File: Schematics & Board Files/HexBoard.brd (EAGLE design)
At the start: 40.4 x 35.6 mm, 26 parts

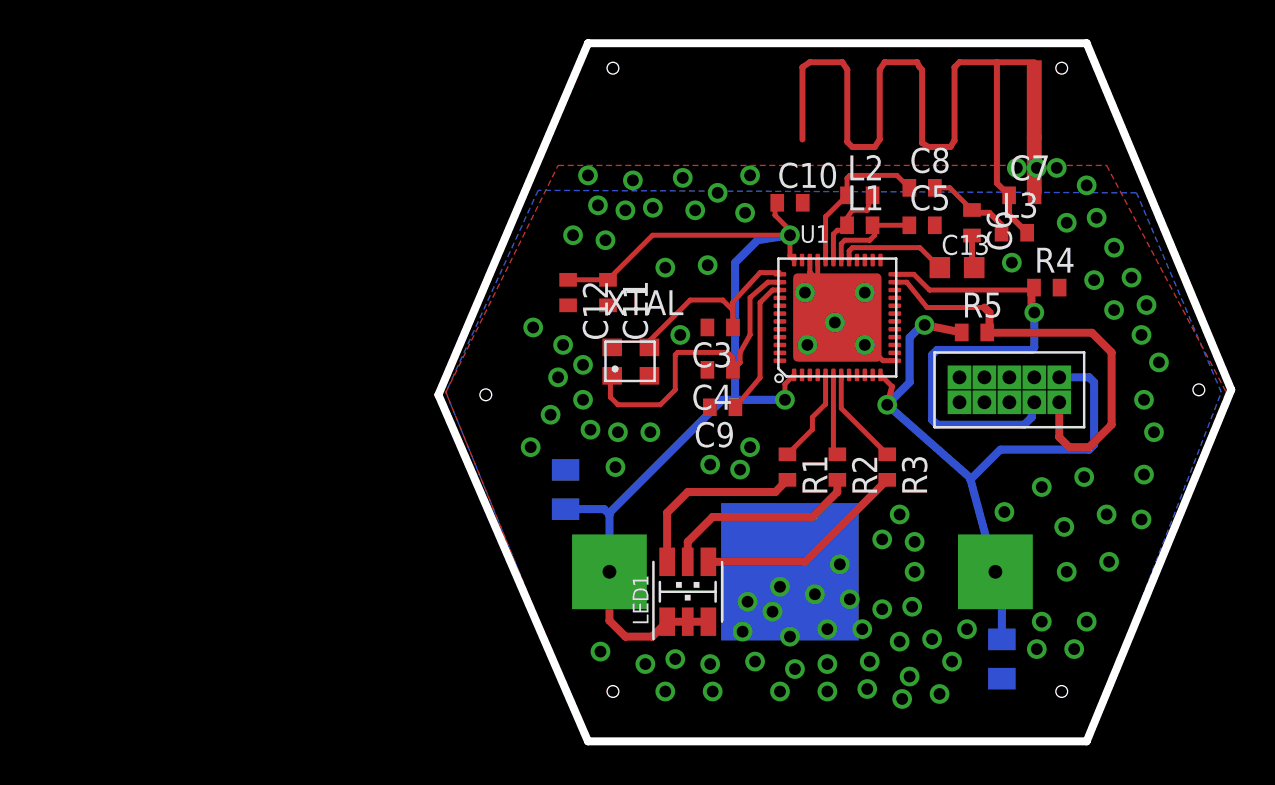
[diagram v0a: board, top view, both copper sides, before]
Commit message: Board and schematic cleanup; see email to Kris today for notes.
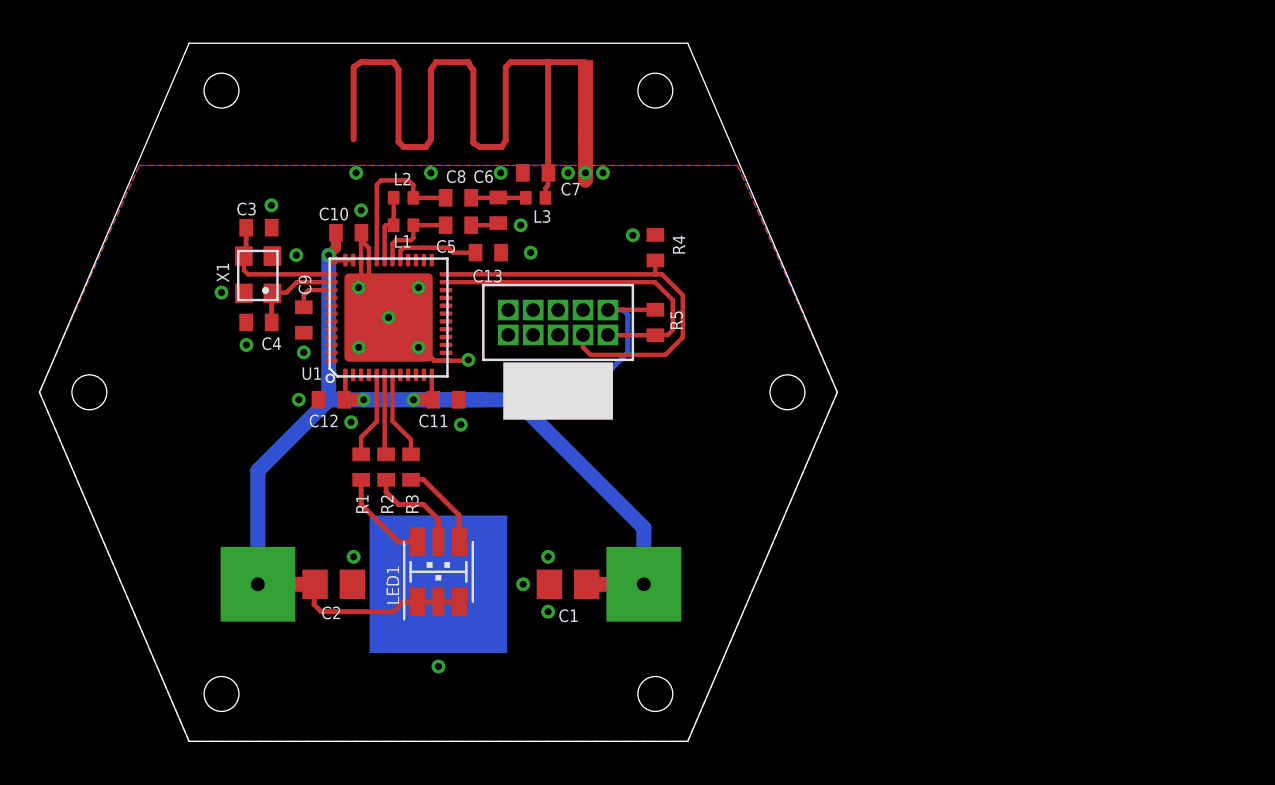
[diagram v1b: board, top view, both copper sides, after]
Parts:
- removed XTAL: TXC-CRYSTAL, TXC:TXC_CRYSTAL
- added X1: TXC-CRYSTAL, TXC:TXC_CRYSTAL
- C1, C2: device adafruit:C0805K -> rcl:C0805
- C10, C11, C12, C3, C4, C5, C6, C7, C8, C9: device adafruit:C0402 -> rcl:C0402
- C13: device adafruit:C0603K -> rcl:C0402
- L1, L2, L3: device CHIP_INDUCTOR:CHIP_INDUCTOR -> rcl_custom:.0402-B-NOSILK
- moved C7 24.8 mm to (25.3, 29.0), turned to 180 degrees
- moved R3 24.3 mm to (18.9, 14.0)
- moved C6 24.1 mm to (23.4, 27.1)
- moved C3 24.0 mm to (11.2, 26.2), turned to 0 degrees
- moved C13 23.9 mm to (22.9, 24.9)
- moved C8 23.6 mm to (21.3, 27.7)
- moved C5 23.6 mm to (21.3, 26.3)
- moved C4 23.6 mm to (11.2, 21.3)
- moved L3 23.5 mm to (25.3, 27.7)
- moved U$1 23.2 mm to (27.7, 22.0)
- moved R2 23.0 mm to (17.7, 14.0)
- moved U1 22.9 mm to (17.8, 21.6)
- moved C10 22.5 mm to (15.7, 25.9)
- moved C1 22.4 mm to (26.9, 8.00), flipped to the top, turned to 180 degrees
- moved L1 22.1 mm to (18.5, 26.3), turned to 180 degrees
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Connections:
- net N$10 renamed !RESET
- net N$7 renamed SWD
- net GND: now also X1.2, X1.4; no longer XTAL.2, XTAL.4
- net N$11: now also L1.2, L2.1; no longer L1.1, L2.2
- net N$15: now also L2.2; no longer L2.1
- net N$17: now also L1.1; no longer L1.2
- net N$8: now also X1.3; no longer XTAL.3
- net N$9: now also X1.1; no longer XTAL.1
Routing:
- net N$9: track 16.2 -> 5.39 mm
- net VDD: track 87.0 -> 78.3 mm, vias 4 -> 3
- net N$3: track 10.8 -> 4.57 mm
- net GND: track 13.0 -> 18.5 mm, vias 99 -> 29
- net !RESET: track 22.3 -> 16.9 mm
- net N$2: track 10.3 -> 5.01 mm
- net N$12: track 7.06 -> 2.12 mm
- net N$1: track 9.33 -> 4.93 mm
- net SWD: track 25.3 -> 21.6 mm, vias 1 -> 0
- net N$8: track 10.1 -> 6.89 mm
- net ANTENNA: track 40.9 -> 38.5 mm
- net N$13: track 4.58 -> 2.79 mm
- net N$18: track 5.58 -> 4.47 mm
- net N$11: track 4.62 -> 3.59 mm
- net N$17: track 5.15 -> 4.54 mm
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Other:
- board size 40.4 x 35.6 mm -> 40.6 x 35.6 mm

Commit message: Latest code latest board and schematic updated maker guide
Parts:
- removed X1: TXC-CRYSTAL, TXC:TXC_CRYSTAL
- added U$2: TXC-CRYSTAL, TXC:TXC_CRYSTAL
- moved LED1 11.4 mm to (10.0, 13.5), turned to 0 degrees
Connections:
- net GND: now also U$2.2, U$2.4; no longer X1.2, X1.4
- net N$8: now also U$2.1; no longer X1.3
- net N$9: now also U$2.3; no longer X1.1
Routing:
- net N$3: track 4.57 -> 11.1 mm
- net VDD: track 78.3 -> 83.7 mm
- net N$2: track 5.01 -> 9.80 mm
- net N$1: track 4.93 -> 8.65 mm
- net N$8: track 6.89 -> 7.42 mm
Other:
- board size 40.6 x 35.6 mm -> 40.5 x 35.6 mm
- board text added: "MIngle Disco Kris Gibbs Brandon Towell 2015"

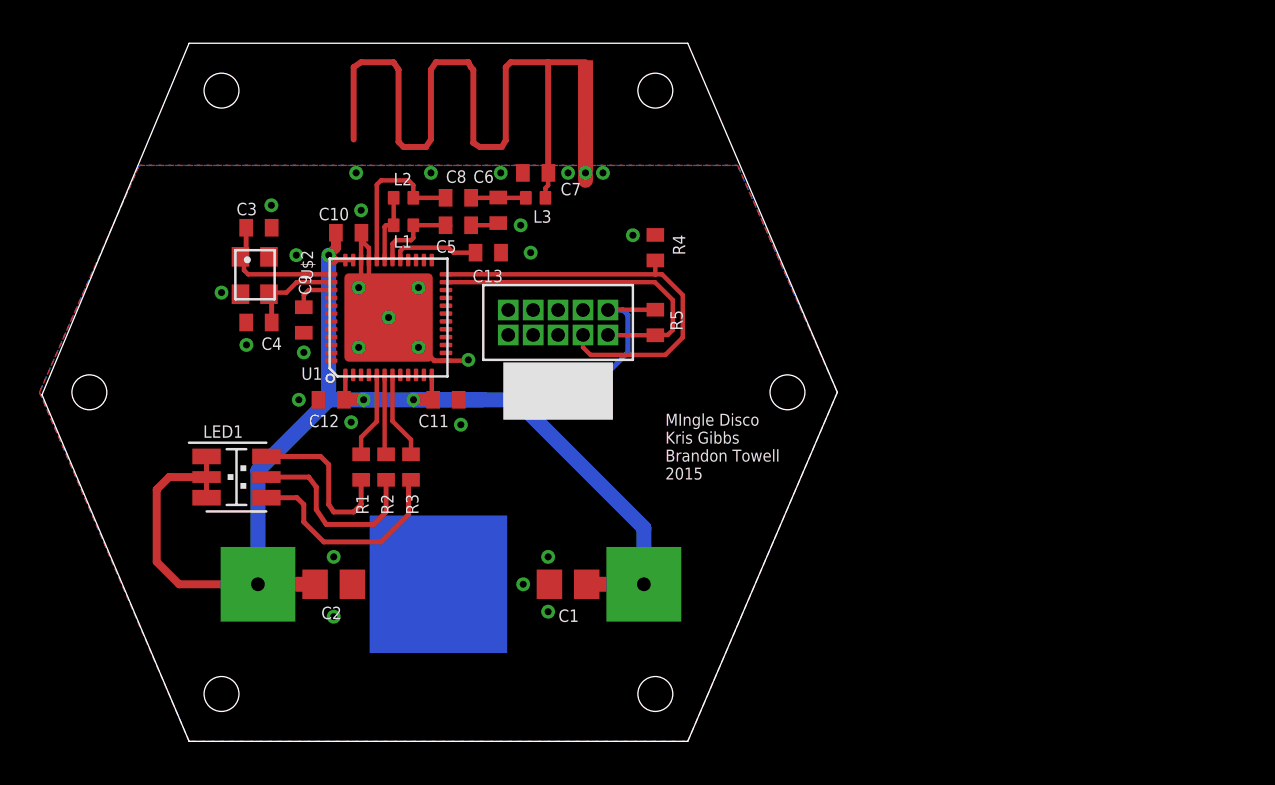
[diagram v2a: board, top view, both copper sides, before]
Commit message: OCD cleaned up of schematic -- nothing different, just prettyness. Cleaned up TNAMES layer a bit on board, checked DRC, moved a few vias... it's good to go. Sending off to OSH Parkgit add HexBoard.brd HexBoard.sch11!
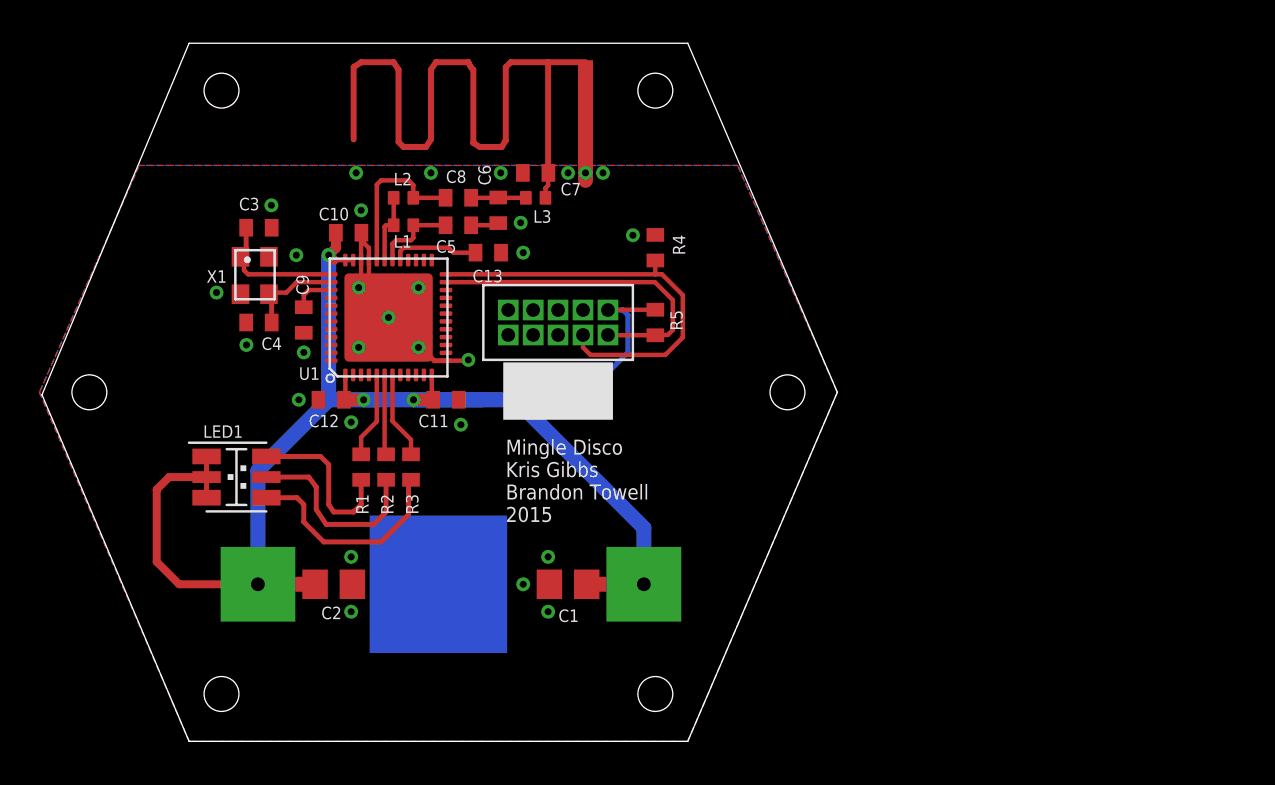
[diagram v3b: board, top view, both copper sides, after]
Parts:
- LED1: value (none) -> SMLV56RGB1W1
- U1: value (none) -> NRF51822-QFAC-R7
- X1: value TXC-CRYSTAL -> 16 MHz
- renumbered U$2 to X1
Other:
- board text added: "Mingle Disco Kris Gibbs Brandon Towell 2015"
- board text removed: "MIngle Disco Kris Gibbs Brandon Towell 2015"
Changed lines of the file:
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@@
 <?xml version="1.0" encoding="utf-8"?>
 <!DOCTYPE eagle SYSTEM "eagle.dtd">
-<eagle version="7.1.0">
+<eagle version="7.3.0">
 <drawing>
 <settings>
@@
 <layer number="14" name="Route14" color="1" fill="6" visible="no" active="yes"/>
 <layer number="15" name="Route15" color="4" fill="6" visible="no" active="yes"/>
-<layer number="16" name="Bottom" color="1" fill="1" visible="yes" active="yes"/>
+<layer number="16" name="Bottom" color="1" fill="1" visible="no" active="yes"/>
 <layer number="17" name="Pads" color="2" fill="1" visible="yes" active="yes"/>
 <layer number="18" name="Vias" color="2" fill="1" visible="yes" active="yes"/>
@@
 <layer number="20" name="Dimension" color="15" fill="1" visible="yes" active="yes"/>
 <layer number="21" name="tPlace" color="7" fill="1" visible="yes" active="yes"/>
-<layer number="22" name="bPlace" color="7" fill="1" visible="yes" active="yes"/>
+<layer number="22" name="bPlace" color="7" fill="1" visible="no" active="yes"/>
 <layer number="23" name="tOrigins" color="15" fill="1" visible="yes" active="yes"/>
 <layer number="24" name="bOrigins" color="15" fill="1" visible="no" active="yes"/>
@@
 <layer number="27" name="tValues" color="7" fill="1" visible="no" active="yes"/>
 <layer number="28" name="bValues" color="7" fill="1" visible="no" active="yes"/>
-<layer number="29" name="tStop" color="7" fill="3" visible="no" active="yes"/>
+<layer number="29" name="tStop" color="7" fill="3" visible="yes" active="yes"/>
 <layer number="30" name="bStop" color="7" fill="6" visible="no" active="yes"/>
 <layer number="31" name="tCream" color="7" fill="4" visible="no" active="yes"/>
@@
 <layer number="44" name="Drills" color="7" fill="1" visible="no" active="yes"/>
 <layer number="45" name="Holes" color="7" fill="1" visible="no" active="yes"/>
-<layer number="46" name="Milling" color="3" fill="1" visible="no" active="yes"/>
+<layer number="46" name="Milling" color="3" fill="1" visible="yes" active="yes"/>
 <layer number="47" name="Measures" color="7" fill="1" visible="no" active="yes"/>
-<layer number="48" name="Document" color="7" fill="1" visible="no" active="yes"/>
+<layer number="48" name="Document" color="7" fill="1" visible="yes" active="yes"/>
 <layer number="49" name="Reference" color="7" fill="1" visible="no" active="yes"/>
 <layer number="50" name="dxf" color="7" fill="1" visible="no" active="no"/>
-<layer number="51" name="tDocu" color="7" fill="1" visible="no" active="yes"/>
+<layer number="51" name="tDocu" color="7" fill="1" visible="yes" active="yes"/>
 <layer number="52" name="bDocu" color="7" fill="1" visible="no" active="yes"/>
 <layer number="53" name="tGND_GNDA" color="7" fill="1" visible="no" active="no"/>
@@
 <wire x1="18.034" y1="19.177" x2="17.526" y2="19.177" width="0" layer="41"/>
 <wire x1="15.367" y1="21.844" x2="15.367" y2="21.336" width="0" layer="41"/>
-<text x="31.877" y="13.335" size="0.6096" layer="25" ratio="20">MIngle Disco
+<text x="23.749" y="11.176" size="0.762" layer="25" ratio="20">Mingle Disco
 Kris Gibbs
 Brandon Towell
@@
 </autorouter>
 <elements>
-<element name="U1" library="nrf51822" package="QFN48-6X6MM" value="" x="17.78" y="21.59" smashed="yes">
-<attribute name="NAME" x="13.335" y="18.415" size="0.635" layer="25" font="vector" ratio="20"/>
+<element name="U1" library="nrf51822" package="QFN48-6X6MM" value="NRF51822-QFAC-R7" x="17.78" y="21.59" smashed="yes">
+<attribute name="NAME" x="13.208" y="18.415" size="0.635" layer="25" font="vector" ratio="20"/>
 <attribute name="VALUE" x="15.911" y="21.598" size="0.635" layer="27" ratio="10"/>
 </element>
-<element name="LED1" library="rgb-led-separate" package="LED-3528" value="" x="10.033" y="13.462" smashed="yes">
+<element name="LED1" library="rgb-led-separate" package="LED-3528" value="SMLV56RGB1W1" x="10.033" y="13.462" smashed="yes">
 <attribute name="NAME" x="8.333" y="15.462" size="0.635" layer="25" font="vector" ratio="20"/>
 <attribute name="VALUE" x="8.333" y="10.662" size="0.8" layer="27" font="vector" ratio="15"/>
@@
 </element>
 <element name="C3" library="rcl" package="C0402" value="12p" x="11.176" y="26.162" smashed="yes">
-<attribute name="NAME" x="10.033" y="26.797" size="0.635" layer="25" font="vector" ratio="20"/>
+<attribute name="NAME" x="10.16" y="27.051" size="0.635" layer="25" font="vector" ratio="20"/>
 <attribute name="VALUE" x="10.541" y="24.257" size="1.27" layer="27"/>
 </element>
@@
 </element>
 <element name="C6" library="rcl" package="C0402" value="1p" x="23.368" y="27.051" smashed="yes" rot="R270">
-<attribute name="NAME" x="22.098" y="28.448" size="0.635" layer="25" font="vector" ratio="20"/>
+<attribute name="NAME" x="22.987" y="28.321" size="0.635" layer="25" font="vector" ratio="20" rot="R90"/>
 <attribute name="VALUE" x="21.463" y="27.686" size="1.27" layer="27" rot="R270"/>
 </element>
@@
 </element>
 <element name="C9" library="rcl" package="C0402" value="100n" x="13.462" y="21.463" smashed="yes" rot="R270">
-<attribute name="NAME" x="13.843" y="22.733" size="0.635" layer="25" font="vector" ratio="20" rot="R90"/>
+<attribute name="NAME" x="13.716" y="22.733" size="0.635" layer="25" font="vector" ratio="20" rot="R90"/>
 <attribute name="VALUE" x="11.557" y="22.098" size="1.27" layer="27" rot="R270"/>
 </element>
@@
 <attribute name="NAME" x="25.273" y="27.686" size="0.2" layer="33" ratio="15" align="center"/>
 </element>
-<element name="U$2" library="TXC" package="TXC_CRYSTAL" value="TXC-CRYSTAL" x="10.795" y="23.749" rot="R270"/>
+<element name="X1" library="TXC" package="TXC_CRYSTAL" value="16 MHz" x="10.795" y="23.749" smashed="yes" rot="R270">
+<attribute name="NAME" x="8.509" y="23.36" size="0.635" layer="25" ratio="20"/>
+<attribute name="VALUE" x="8.747" y="25.019" size="0.6096" layer="27" rot="R270"/>
+</element>
 </elements>
 <signals>
@@
 <wire x1="27.813" y1="31.115" x2="27.813" y2="28.575" width="0.762" layer="1"/>
 <wire x1="16.256" y1="20.066" x2="17.78" y2="21.59" width="0.254" layer="1"/>
-<via x="24.511" y="26.289" extent="1-16" drill="0.3556"/>
-<via x="25.019" y="24.892" extent="1-16" drill="0.3556"/>
+<via x="24.511" y="26.416" extent="1-16" drill="0.3556"/>
+<via x="24.638" y="24.892" extent="1-16" drill="0.3556"/>
 <via x="23.495" y="28.956" extent="1-16" drill="0.3556"/>
 <via x="19.939" y="28.956" extent="1-16" drill="0.3556"/>
@@
 <via x="13.081" y="24.765" extent="1-16" drill="0.3556"/>
 <via x="11.811" y="27.305" extent="1-16" drill="0.3556"/>
-<via x="9.271" y="22.86" extent="1-16" drill="0.3556"/>
+<via x="9.017" y="22.86" extent="1-16" drill="0.3556"/>
 <via x="10.541" y="20.193" extent="1-16" drill="0.3556"/>
 <via x="13.462" y="19.812" extent="1-16" drill="0.3556"/>
@@
 <via x="24.638" y="8.001" extent="1-16" drill="0.3556"/>
 <via x="25.908" y="6.604" extent="1-16" drill="0.3556"/>
-<via x="14.986" y="6.35" extent="1-16" drill="0.3556"/>
-<via x="14.986" y="9.398" extent="1-16" drill="0.3556"/>
-<contactref element="U$2" pad="2"/>
-<contactref element="U$2" pad="4"/>
+<via x="15.875" y="6.604" extent="1-16" drill="0.3556"/>
+<via x="15.875" y="9.398" extent="1-16" drill="0.3556"/>
+<contactref element="X1" pad="2"/>
+<contactref element="X1" pad="4"/>
 </signal>
 <signal name="N$8">
@@
 <wire x1="10.627" y1="23.79" x2="10.414" y2="24.003" width="0.2286" layer="1"/>
 <wire x1="10.414" y1="24.003" x2="10.414" y2="24.716" width="0.2286" layer="1"/>
-<contactref element="U$2" pad="1"/>
+<contactref element="X1" pad="1"/>
 <wire x1="10.237" y1="24.679" x2="10.343" y2="24.933" width="0.254" layer="1"/>
 <wire x1="10.343" y1="24.933" x2="10.526" y2="24.75" width="0.254" layer="1"/>
@@
 <wire x1="11.826" y1="21.336" x2="11.826" y2="22.894" width="0.254" layer="1"/>
 <wire x1="11.521" y1="22.86" x2="11.521" y2="22.867" width="0.254" layer="1"/>
-<contactref element="U$2" pad="3"/>
+<contactref element="X1" pad="3"/>
 <wire x1="11.521" y1="22.86" x2="11.606" y2="22.86" width="0.254" layer="1"/>
 <wire x1="11.606" y1="22.86" x2="11.687" y2="22.779" width="0.254" layer="1"/>
